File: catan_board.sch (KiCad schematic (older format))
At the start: 28 parts

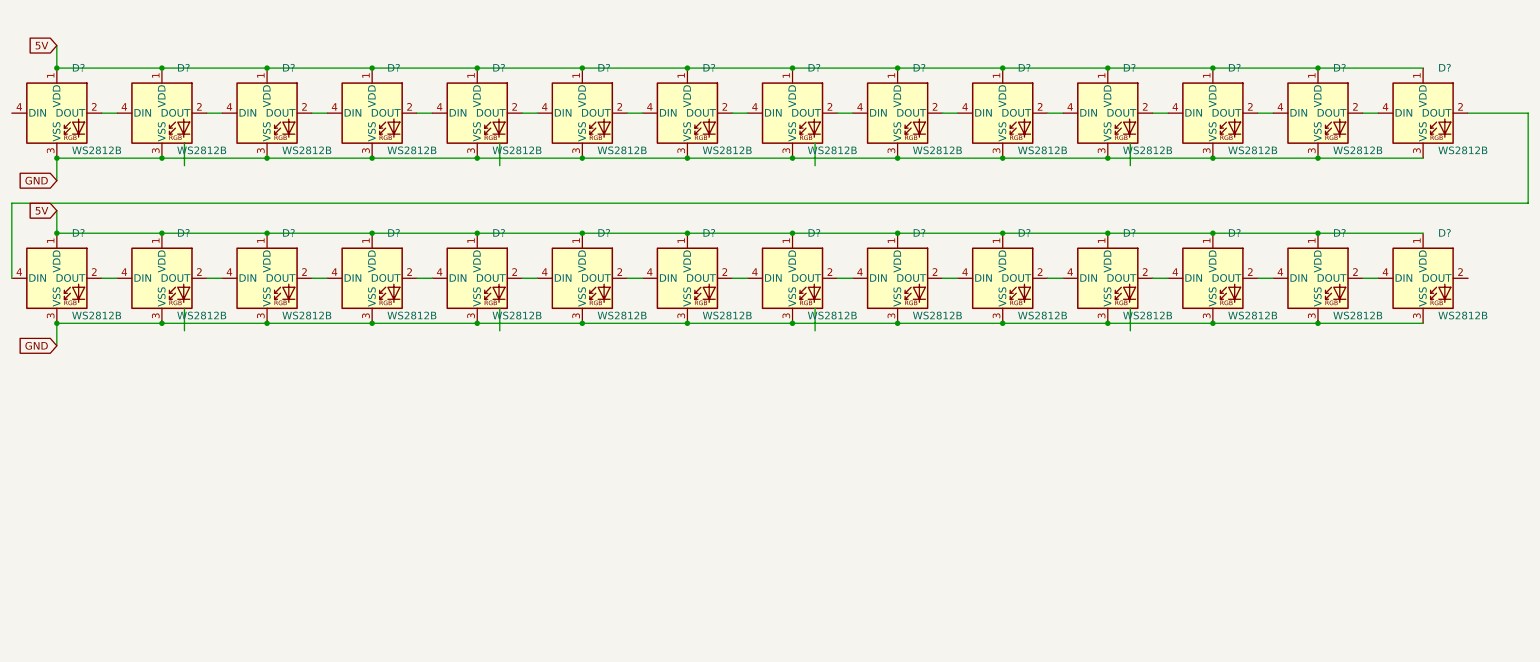
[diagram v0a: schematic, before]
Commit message: gnd pour done, maybe should add 5v rail on other side
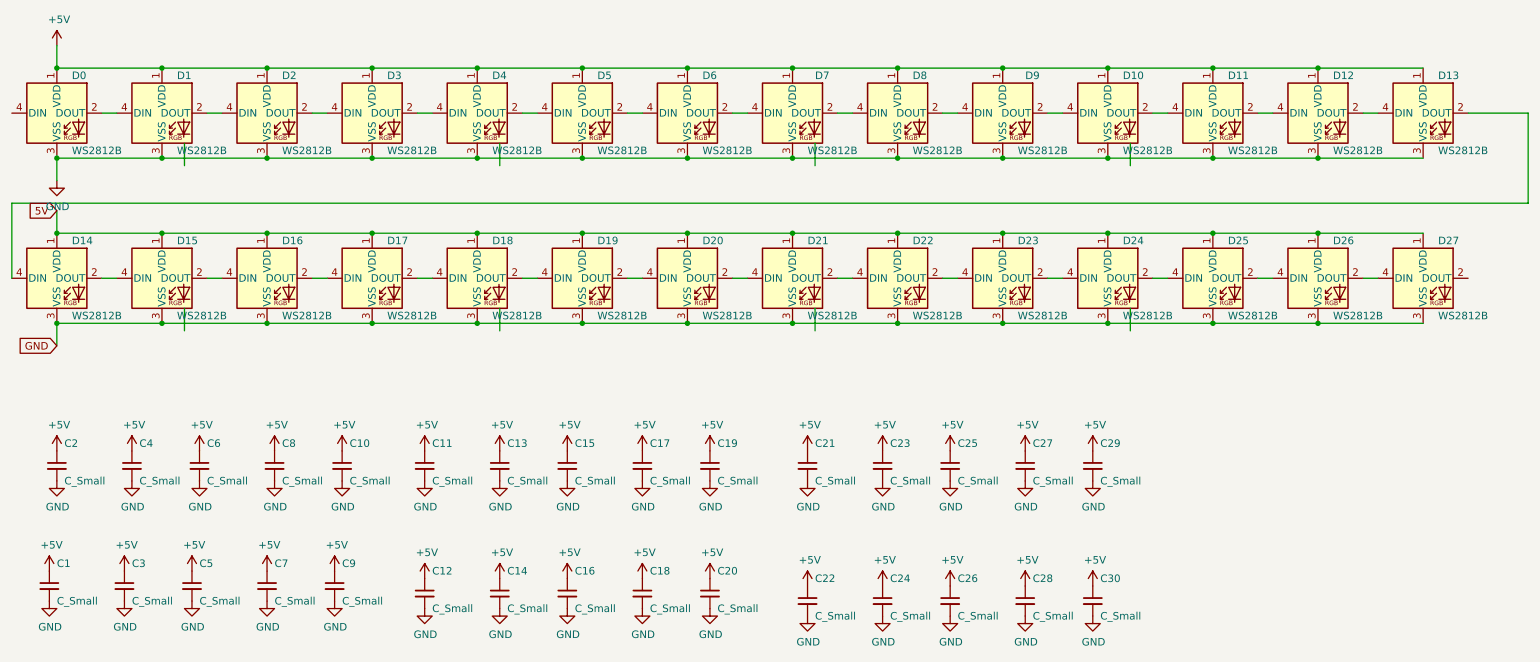
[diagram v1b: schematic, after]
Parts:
- added C1, C10, C11, C12, C13, C14, C15, C16, C17, C18, C19, C2, C20, C21, C22, C23, C24, C25, C26, C27, C28, C29, C3, C30, C4, C5, C6, C7, C8, C9: C_Small, Capacitor_SMD:C_0805_2012Metric_Pad1.18x1.45mm_HandSolder, symbol Device:C_Small
- gave numbers to parts that had none: 28
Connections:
- net labels added: +5V
